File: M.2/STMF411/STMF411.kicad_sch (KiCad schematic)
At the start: 26 parts, among them M1 M.2_Key_E, Q1 2N7002, SW1 RESET, U1 XC6206P332MR, U2 STM32F411CCUx, Y1 16 MHz

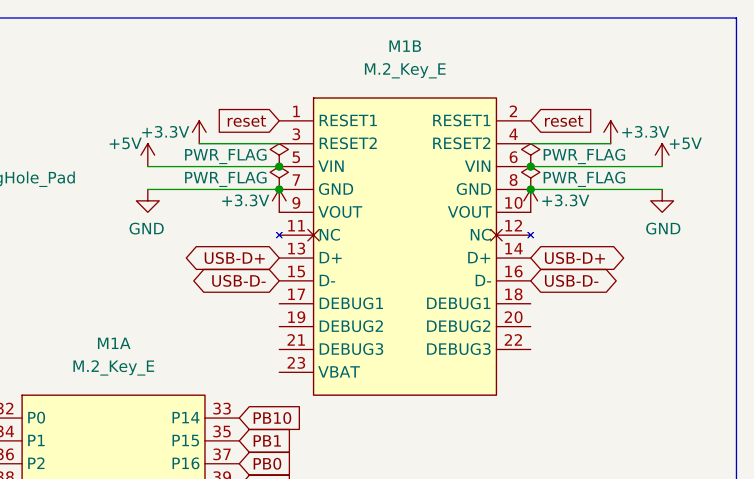
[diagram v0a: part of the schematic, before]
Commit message: change stm to use 5v instead of 3.3v on vout
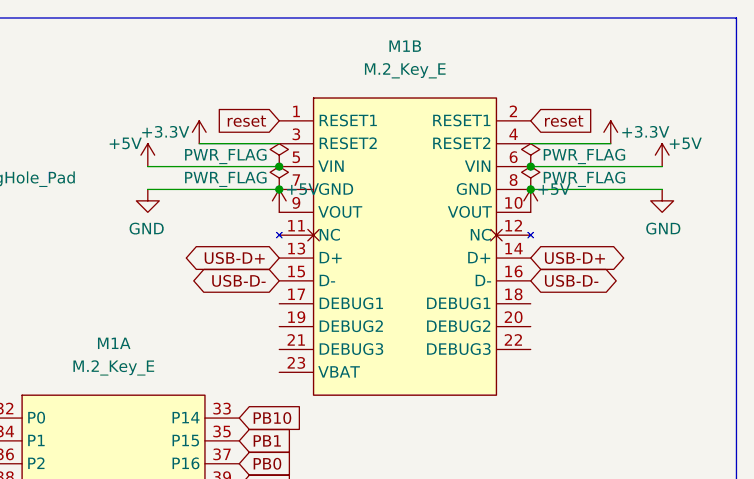
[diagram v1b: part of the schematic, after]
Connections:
- net +3V3: no longer M1.10 (VOUT), M1.9 (VOUT)
- net +5V: now also M1.10 (VOUT), M1.9 (VOUT)
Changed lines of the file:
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@@
     (pin "2")
-  )
-  (symbol (lib_id "power:+3.3V") (at 233.045 34.925 0) (mirror y) (unit 1)
-    (in_bom yes) (on_board yes)
-    (property "Reference" "#PWR0102" (id 0) (at 233.045 38.735 0)
-      (effects (font (size 1.27 1.27)) hide)
-    )
-    (property "Value" "+3.3V" (id 1) (at 229.235 33.655 0))
-    (property "Footprint" "" (id 2) (at 233.045 34.925 0)
-      (effects (font (size 1.27 1.27)) hide)
-    )
-    (property "Datasheet" "" (id 3) (at 233.045 34.925 0)
-      (effects (font (size 1.27 1.27)) hide)
-    )
-    (pin "1")
   )
   (symbol (lib_id "Device:R_Small") (at 80.645 34.925 0) (unit 1)
@@
     (pin "9")
   )
+  (symbol (lib_id "power:+5V") (at 260.985 34.925 0) (unit 1)
+    (in_bom yes) (on_board yes)
+    (property "Reference" "#PWR?" (id 0) (at 260.985 38.735 0)
+      (effects (font (size 1.27 1.27)) hide)
+    )
+    (property "Value" "+5V" (id 1) (at 263.525 32.385 0))
+    (property "Footprint" "" (id 2) (at 260.985 34.925 0)
+      (effects (font (size 1.27 1.27)) hide)
+    )
+    (property "Datasheet" "" (id 3) (at 260.985 34.925 0)
+      (effects (font (size 1.27 1.27)) hide)
+    )
+    (pin "1")
+  )
   (symbol (lib_id "Power:GND") (at 191.135 33.655 0) (unit 1)
     (in_bom yes) (on_board yes)
@@
     )
     (property "Datasheet" "" (id 3) (at 68.58 93.98 0)
-      (effects (font (size 1.27 1.27)) hide)
-    )
-    (pin "1")
-  )
-  (symbol (lib_id "power:+3.3V") (at 260.985 34.925 0) (unit 1)
-    (in_bom yes) (on_board yes)
-    (property "Reference" "#PWR0122" (id 0) (at 260.985 38.735 0)
-      (effects (font (size 1.27 1.27)) hide)
-    )
-    (property "Value" "+3.3V" (id 1) (at 264.795 33.655 0))
-    (property "Footprint" "" (id 2) (at 260.985 34.925 0)
-      (effects (font (size 1.27 1.27)) hide)
-    )
-    (property "Datasheet" "" (id 3) (at 260.985 34.925 0)
       (effects (font (size 1.27 1.27)) hide)
     )
@@
     (pin "2")
   )
+  (symbol (lib_id "power:+5V") (at 233.045 34.925 0) (unit 1)
+    (in_bom yes) (on_board yes)
+    (property "Reference" "#PWR?" (id 0) (at 233.045 38.735 0)
+      (effects (font (size 1.27 1.27)) hide)
+    )
+    (property "Value" "+5V" (id 1) (at 235.585 32.385 0))
+    (property "Footprint" "" (id 2) (at 233.045 34.925 0)
+      (effects (font (size 1.27 1.27)) hide)
+    )
+    (property "Datasheet" "" (id 3) (at 233.045 34.925 0)
+      (effects (font (size 1.27 1.27)) hide)
+    )
+    (pin "1")
+  )
   (symbol (lib_id "power:+3.3V") (at 269.875 27.305 0) (unit 1)
     (in_bom yes) (on_board yes)
@@
       (reference "#PWR0101") (unit 1) (value "GND") (footprint "")
     )
-    (path "/a27efb68-393b-4108-b030-887c6f153a57"
-      (reference "#PWR0102") (unit 1) (value "+3.3V") (footprint "")
-    )
     (path "/581c7a64-fba5-4d4a-824b-f49a62311590"
       (reference "#PWR0103") (unit 1) (value "+3.3V") (footprint "")
@@
       (reference "#PWR0121") (unit 1) (value "GND") (footprint "")
     )
-    (path "/c658c311-c7f5-4b2d-a661-b079120876a8"
-      (reference "#PWR0122") (unit 1) (value "+3.3V") (footprint "")
+    (path "/a818dbd6-8d05-4bed-8e76-065b136c4a97"
+      (reference "#PWR?") (unit 1) (value "+5V") (footprint "")
+    )
+    (path "/df2e1f24-b744-41fa-a600-538bf3e9f386"
+      (reference "#PWR?") (unit 1) (value "+5V") (footprint "")
     )
     (path "/42ec88f7-d7f3-40cf-8759-f8c5477df41e"

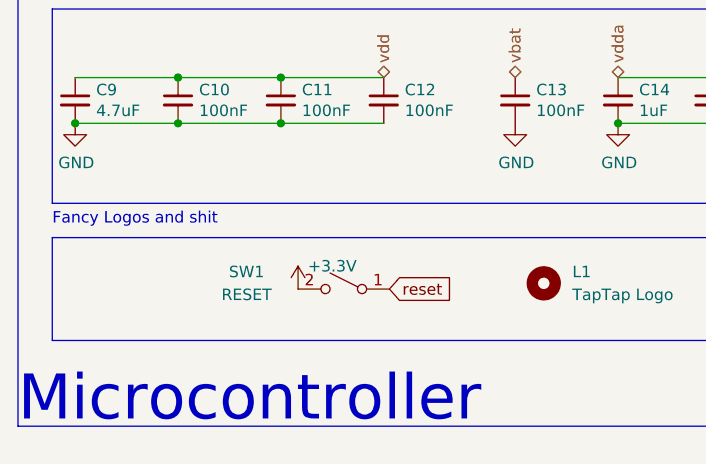
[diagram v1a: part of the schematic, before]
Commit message: change modules to new logo
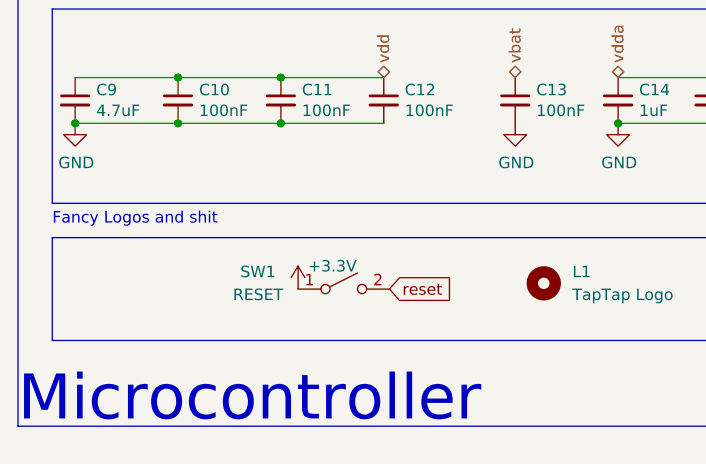
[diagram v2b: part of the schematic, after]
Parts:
- SW1: footprint LogoSmall:LogoSmall -> (none)
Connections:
- net +3V3: now also SW1.1 (A); no longer SW1.2 (B)
- net BOOT0: now also SW1.2 (B); no longer SW1.1 (A)
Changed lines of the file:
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@@
     (pin "74")
     (pin "75")
+    (pin "1")
+    (pin "10")
+    (pin "11")
+    (pin "12")
+    (pin "13")
+    (pin "14")
+    (pin "15")
+    (pin "16")
+    (pin "17")
+    (pin "18")
+    (pin "19")
+    (pin "2")
+    (pin "20")
+    (pin "21")
+    (pin "22")
+    (pin "23")
+    (pin "24")
+    (pin "3")
+    (pin "4")
+    (pin "5")
+    (pin "6")
+    (pin "7")
+    (pin "8")
+    (pin "9")
   )
   (symbol (lib_id "Device:C_Small") (at 34.925 66.04 0) (unit 1)
@@
     (pin "1")
   )
-  (symbol (lib_id "Switch:SW_SPST") (at 49.53 112.395 0) (mirror y) (unit 1)
-    (in_bom yes) (on_board yes)
-    (property "Reference" "SW1" (id 0) (at 38.735 110.49 0))
-    (property "Value" "RESET" (id 1) (at 38.735 113.03 0))
-    (property "Footprint" "LogoSmall:LogoSmall" (id 2) (at 49.53 112.395 0)
+  (symbol (lib_id "Switch:SW_SPST") (at 49.53 112.395 0) (unit 1)
+    (in_bom yes) (on_board yes)
+    (property "Reference" "SW1" (id 0) (at 40.005 110.49 0))
+    (property "Value" "RESET" (id 1) (at 40.005 113.03 0))
+    (property "Footprint" "" (id 2) (at 49.53 112.395 0)
       (effects (font (size 1.27 1.27)) hide)
     )
@@
   (symbol (lib_id "power:+5V") (at 260.985 34.925 0) (unit 1)
     (in_bom yes) (on_board yes)
-    (property "Reference" "#PWR?" (id 0) (at 260.985 38.735 0)
+    (property "Reference" "#PWR0111" (id 0) (at 260.985 38.735 0)
       (effects (font (size 1.27 1.27)) hide)
     )
@@
       (effects (font (size 1.27 1.27)) hide)
     )
+    (pin "32")
+    (pin "33")
+    (pin "34")
+    (pin "35")
+    (pin "36")
+    (pin "37")
+    (pin "38")
+    (pin "39")
+    (pin "40")
+    (pin "41")
+    (pin "42")
+    (pin "43")
+    (pin "44")
+    (pin "45")
+    (pin "46")
+    (pin "47")
+    (pin "48")
+    (pin "49")
+    (pin "50")
+    (pin "51")
+    (pin "52")
+    (pin "53")
+    (pin "54")
+    (pin "55")
+    (pin "56")
+    (pin "57")
+    (pin "58")
+    (pin "59")
+    (pin "60")
+    (pin "61")
+    (pin "62")
+    (pin "63")
+    (pin "64")
+    (pin "65")
+    (pin "66")
+    (pin "67")
+    (pin "68")
+    (pin "69")
+    (pin "70")
+    (pin "71")
+    (pin "72")
+    (pin "73")
+    (pin "74")
+    (pin "75")
     (pin "1")
     (pin "10")
@@
   (symbol (lib_id "power:+5V") (at 233.045 34.925 0) (unit 1)
     (in_bom yes) (on_board yes)
-    (property "Reference" "#PWR?" (id 0) (at 233.045 38.735 0)
+    (property "Reference" "#PWR0102" (id 0) (at 233.045 38.735 0)
       (effects (font (size 1.27 1.27)) hide)
     )
@@
       (reference "#PWR0101") (unit 1) (value "GND") (footprint "")
     )
+    (path "/df2e1f24-b744-41fa-a600-538bf3e9f386"
+      (reference "#PWR0102") (unit 1) (value "+5V") (footprint "")
+    )
     (path "/581c7a64-fba5-4d4a-824b-f49a62311590"
       (reference "#PWR0103") (unit 1) (value "+3.3V") (footprint "")
@@
       (reference "#PWR0110") (unit 1) (value "GND") (footprint "")
     )
+    (path "/a818dbd6-8d05-4bed-8e76-065b136c4a97"
+      (reference "#PWR0111") (unit 1) (value "+5V") (footprint "")
+    )
     (path "/e713c566-376a-4c0f-ba8a-6479863d15b8"
       (reference "#PWR0113") (unit 1) (value "+3.3V") (footprint "")
@@
       (reference "#PWR0121") (unit 1) (value "GND") (footprint "")
     )
-    (path "/a818dbd6-8d05-4bed-8e76-065b136c4a97"
-      (reference "#PWR?") (unit 1) (value "+5V") (footprint "")
-    )
-    (path "/df2e1f24-b744-41fa-a600-538bf3e9f386"
-      (reference "#PWR?") (unit 1) (value "+5V") (footprint "")
-    )
     (path "/42ec88f7-d7f3-40cf-8759-f8c5477df41e"
       (reference "C1") (unit 1) (value "4.7uF") (footprint "Capacitor_SMD:C_0402_1005Metric")
@@
     )
     (path "/7cf0f891-8a1a-40d2-a263-a0d273d44d57"
-      (reference "SW1") (unit 1) (value "RESET") (footprint "LogoSmall:LogoSmall")
+      (reference "SW1") (unit 1) (value "RESET") (footprint "LogoSmall:LogoSmall_Cu")
     )
     (path "/7dbb2fc9-ee7c-4a13-a074-2dbb8ae45f20"

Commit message: prettify files a lil bit
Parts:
- SW1: footprint (none) -> LogoSmall:LogoSmall_Cu
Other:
- company: (none) -> Taptap
- title: (none) -> StmF411 Module
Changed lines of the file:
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@@
 (kicad_sch (version 20211123) (generator eeschema)
   (paper "A4")
+  (title_block
+    (title "StmF411 Module")
+    (date "2022-03-26")
+    (rev "1")
+    (company "Taptap")
+  )
   (junction (at 139.065 109.855) (diameter 0) (color 0 0 0 0)
   )
@@
     (property "Reference" "SW1" (id 0) (at 40.005 110.49 0))
     (property "Value" "RESET" (id 1) (at 40.005 113.03 0))
-    (property "Footprint" "" (id 2) (at 49.53 112.395 0)
-      (effects (font (size 1.27 1.27)) hide)
-    )
+    (property "Footprint" "LogoSmall:LogoSmall_Cu" (id 2) (at 49.53 112.395 0)
+      (effects (font (size 1.27 1.27)) hide)
+    )
